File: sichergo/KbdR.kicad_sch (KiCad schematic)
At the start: 21 parts, among them J2 Conn_01x04_Pin, SW2 SW_Push_DPDT, U7 YTS1C0033BBG01, U8 STM32F103C8Tx, Y2 Crystal_GND24

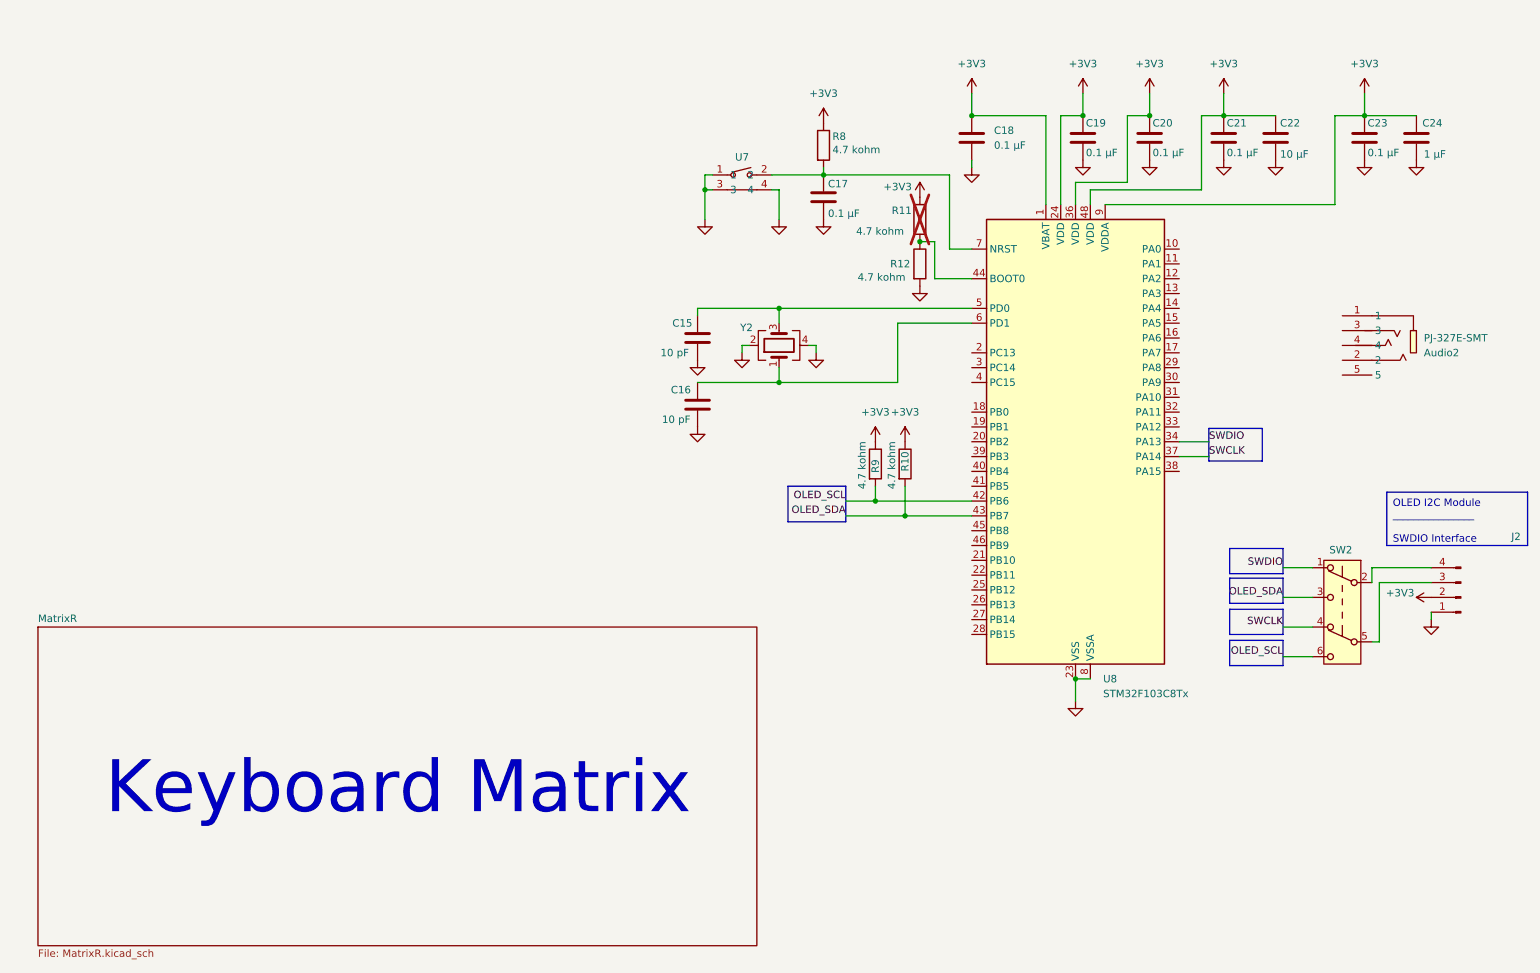
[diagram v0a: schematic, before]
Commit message: Added initial matrix and UART
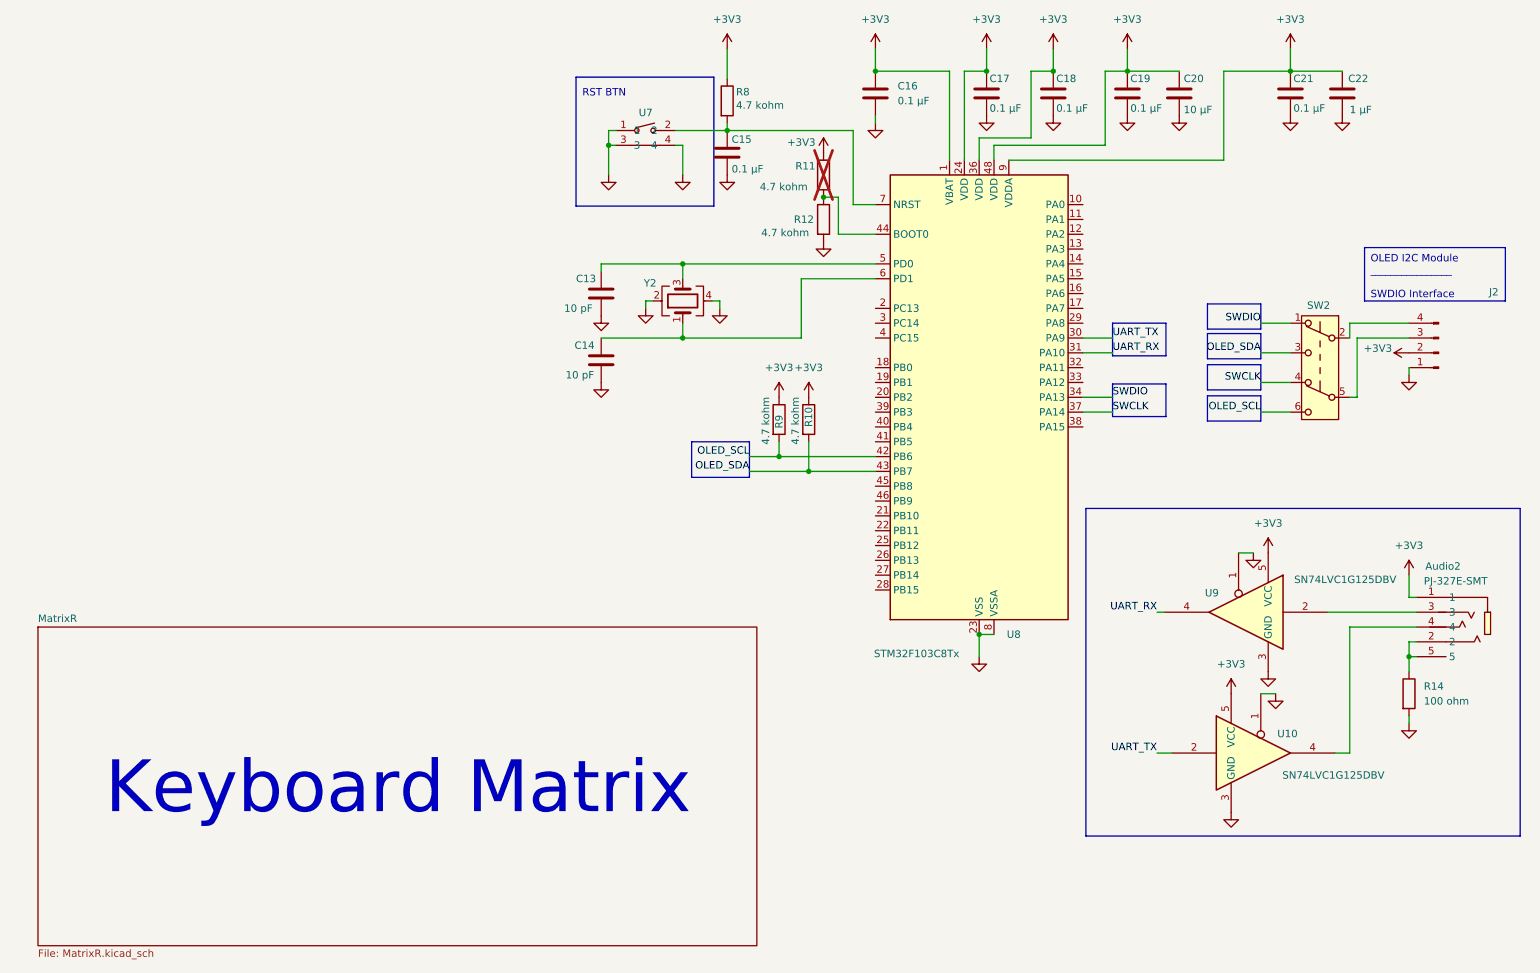
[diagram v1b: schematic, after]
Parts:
- removed C15, C16: 10 pF, 0805 (2012 Metric), symbol #inventree:CL21C100CBANNNC
- removed C20, C23: 0.1 µF, 0805 (2012 Metric), symbol #inventree:CL21B104KBCNNNC
- removed C22: 10 µF, 0805 (2012 Metric), symbol #inventree:CL21A106KOQNNNE
- removed C24: 1 µF, 0805 (2012 Metric), symbol #inventree:CL21B105KAFNNNE
- added C13, C14: 10 pF, 0805 (2012 Metric), symbol #inventree:CL21C100CBANNNC
- added C15, C16: 0.1 µF, 0805 (2012 Metric), symbol #inventree:CL21B104KBCNNNC
- added C20: 10 µF, 0805 (2012 Metric), symbol #inventree:CL21A106KOQNNNE
- added C22: 1 µF, 0805 (2012 Metric), symbol #inventree:CL21B105KAFNNNE
- added R14: 100 ohm, Resistor_SMD:R_0805_2012Metric_Pad1.20x1.40mm_HandSolder, symbol #inventree:ERJ-6GEYJ101V
- added U10, U9: SN74LVC1G125DBV, Package_TO_SOT_SMD:SOT-23-5_HandSoldering, symbol 74xGxx:SN74LVC1G125DBV
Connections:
- net +3V3: now also Audio2.1, C17.1, C16.1, C20.1, C22.1, U10.5 (VCC), U9.5 (VCC)
- net GND: now also C13.2, C14.2, C15.2, C16.2, C20.2, C22.2, R14.2, U10.1, U10.3 (GND), U9.1, U9.3 (GND)
- net UART_TX: now reaches U8.30 (PA9)
- net UART_TX: now also U10.2
- net UART_RX: now reaches U8.31 (PA10)
- net UART_RX: now also U9.4
- net at U8.5 (PD0), Y2.3: now also C13.1
- net at U8.6 (PD1), Y2.1: now also C14.1
- net at R8.2, U7.2, U8.7 (NRST): now also C15.1; no longer C17.1
- net at Audio2.2: now also Audio2.5, R14.1
- net at Audio2.3: now also U9.2
- net at Audio2.4: now also U10.4
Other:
- note added: "RST BTN"

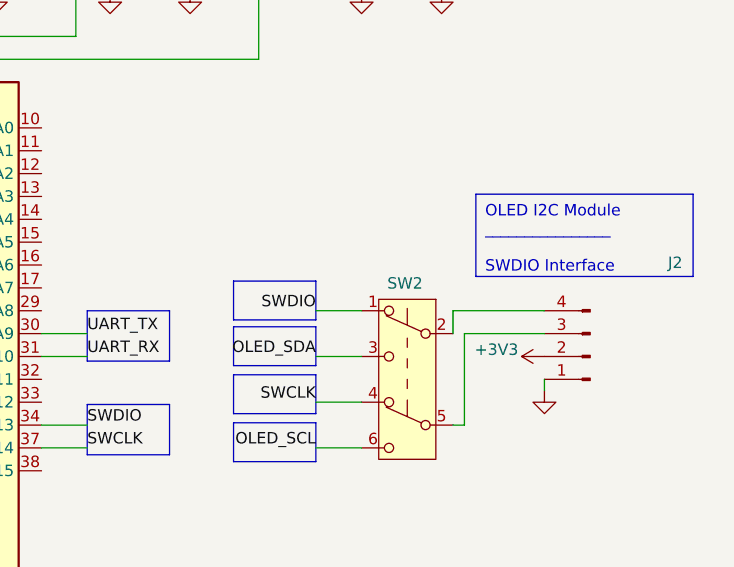
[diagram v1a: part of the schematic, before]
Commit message: Added footprints to switches
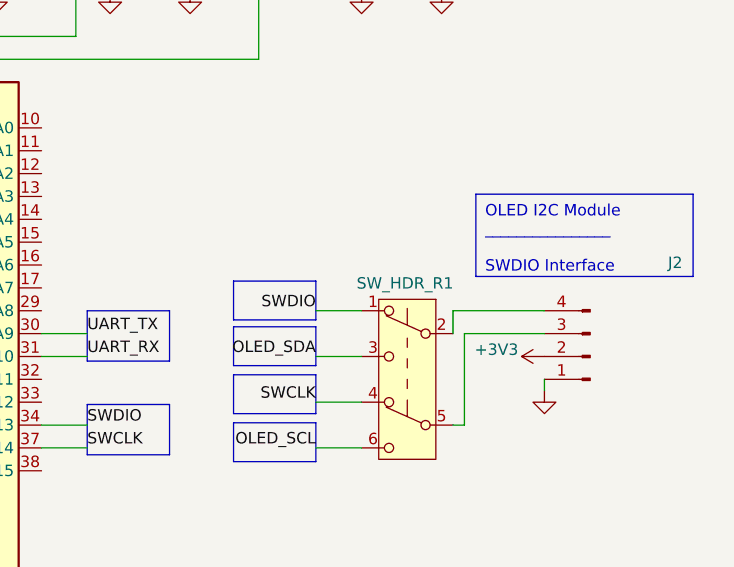
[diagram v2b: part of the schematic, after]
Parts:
- U10, U9: InvenTree (none) -> 66
- renumbered SW2 to SW_HDR_R1
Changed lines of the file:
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@@
 		(on_board yes)
 		(dnp no)
-		(property "Reference" "SW2"
+		(property "Reference" "SW_HDR_R1"
 			(at 241.046 69.342 0)
 			(effects
@@
 			(project "sichergo"
 				(path "/7d6715fb-1e77-4b7f-bc05-ec156d7f2ccd/006ad525-0e9b-4dbe-bfc5-b6bb7b59b94a"
-					(reference "SW2")
+					(reference "SW_HDR_R1")
 					(unit 1)
 				)
@@
 			)
 		)
+		(property "InvenTree" "66"
+			(at 231.14 146.05 0)
+			(effects
+				(font
+					(size 1.27 1.27)
+				)
+				(hide yes)
+			)
+		)
 		(pin "1"
 		)
@@
 			(at 227.33 121.92 0)
 			(effects
+				(font
+					(size 1.27 1.27)
+				)
+				(hide yes)
+			)
+		)
+		(property "InvenTree" "66"
+			(at 227.33 121.92 0)
+			(effects

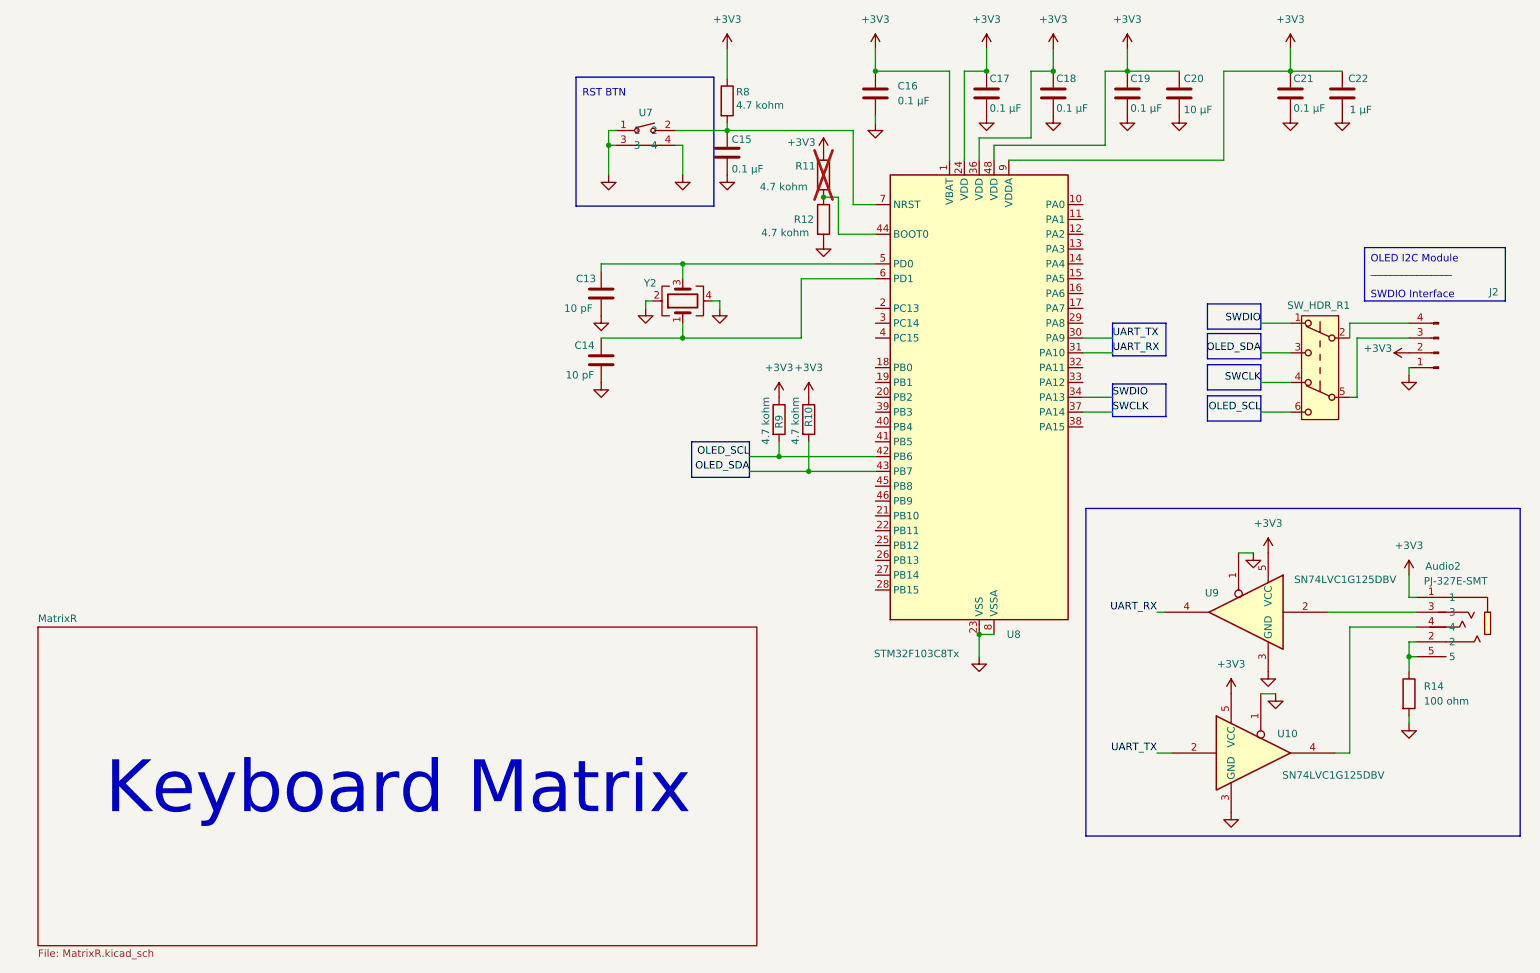
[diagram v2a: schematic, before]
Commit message: Add backlight and switch connections
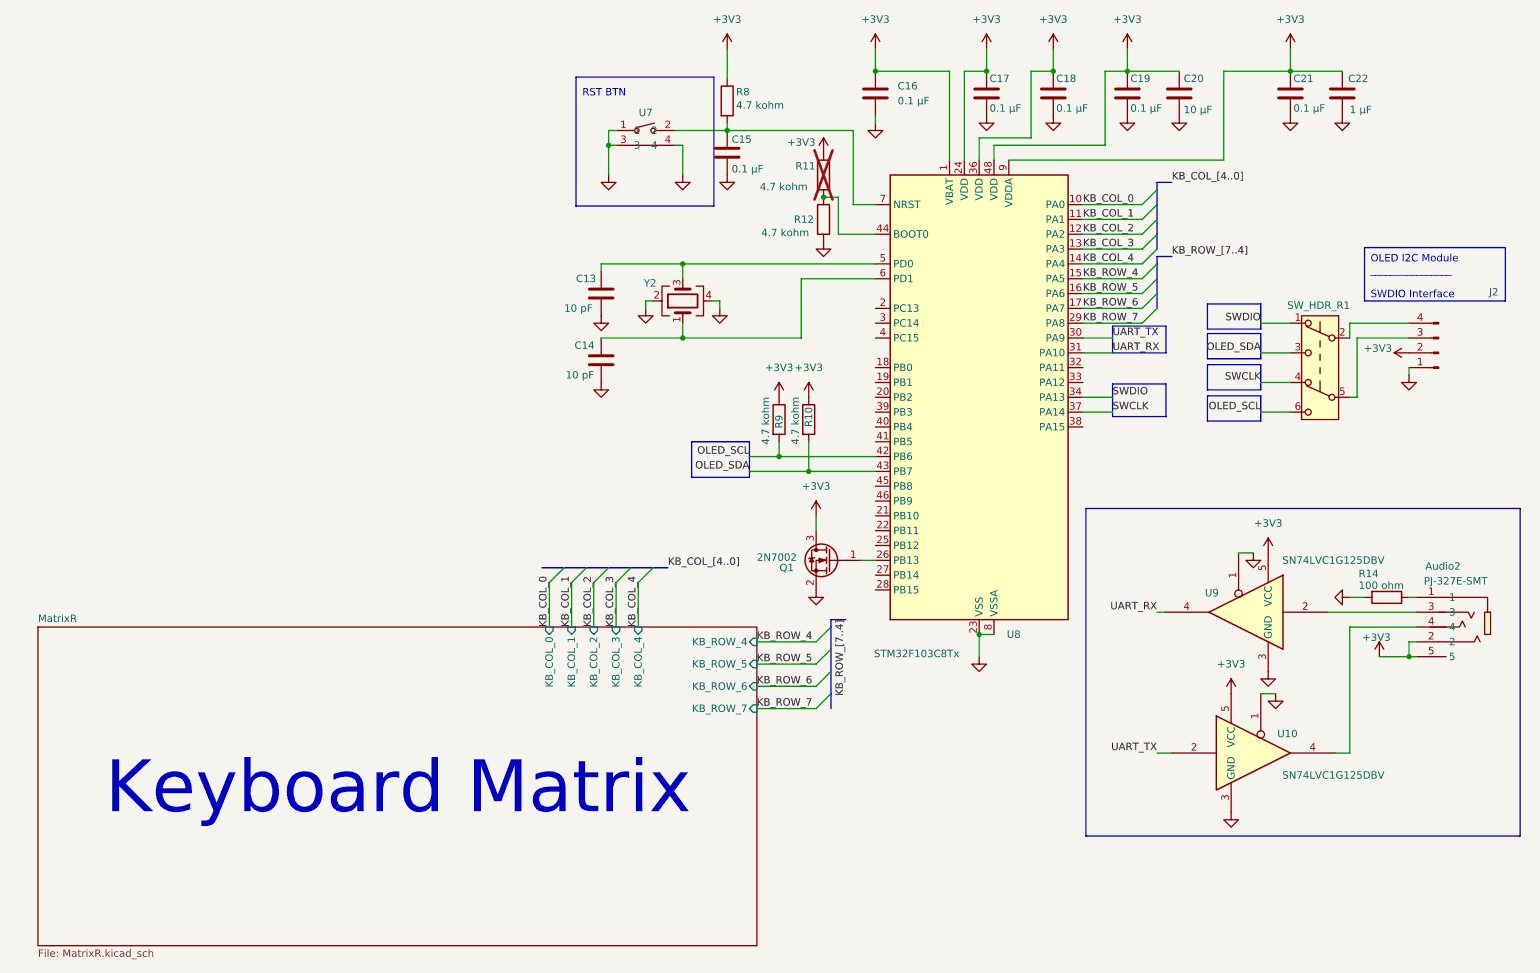
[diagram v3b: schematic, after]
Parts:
- added Q1: 2N7002, Package_TO_SOT_SMD:SOT-23_Handsoldering, symbol Transistor_FET:2N7002
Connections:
- net +3V3: now also Audio2.2, Audio2.5, Q1.3 (D); no longer Audio2.1
- net GND: now also Q1.2 (S)
- net KB_COL_0: now reaches U8.10 (PA0)
- net KB_COL_1: now reaches U8.11 (PA1)
- net KB_COL_2: now reaches U8.12 (PA2)
- net KB_COL_3: now reaches U8.13 (PA3)
- net KB_COL_4: now reaches U8.14 (PA4)
- net KB_ROW_4: now reaches U8.15 (PA5)
- net KB_ROW_5: now reaches U8.16 (PA6)
- net KB_ROW_6: now reaches U8.17 (PA7)
- net at U8.26 (PB13): now also Q1.1 (G)
- net KB_ROW_7: now reaches U8.29 (PA8)
- new net: Audio2.1, R14.1
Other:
- sheet MatrixR ports: added KB_COL_0, KB_COL_1, KB_COL_2, KB_COL_3, KB_COL_4, KB_ROW_4, KB_ROW_5, KB_ROW_6, KB_ROW_7; removed none

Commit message: Pre finish layout
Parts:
- added R52: 5.1 kohm, Resistor_SMD:R_0612_1632Metric_Pad1.18x3.40mm_HandSolder, symbol #inventree:RC0603FR-075K1L
- Q1: InvenTree (none) -> 68
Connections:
- net GND: now also R52.2
- net at Q1.1 (G), U8.26 (PB13): now also R52.1
- no-connect marks 0 -> 19
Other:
- sheet MatrixR ports: added LED_DRIVE; removed none
